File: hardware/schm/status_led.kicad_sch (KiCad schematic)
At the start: 9 parts, among them U10 SK9822-EC20, U8 SN74AHCT1G125, U9 SN74AHCT1G125

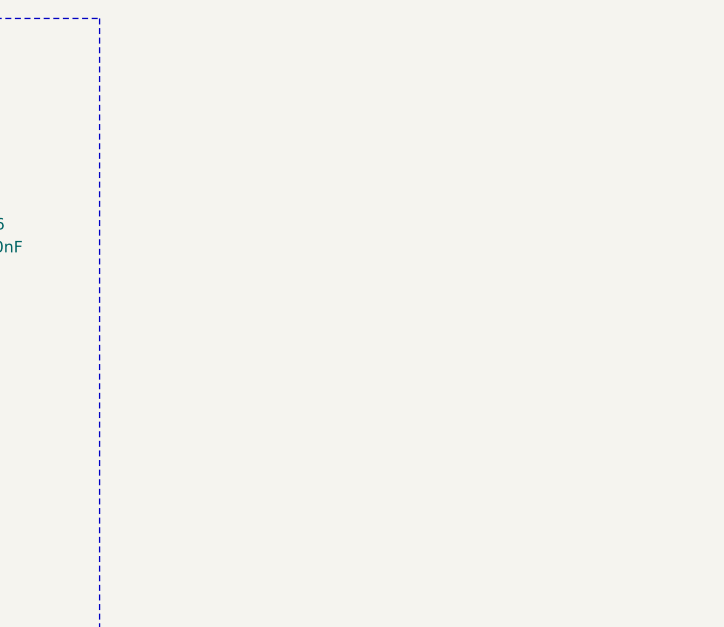
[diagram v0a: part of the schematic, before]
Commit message: feat: swap to the 74HC595 for cs expansion
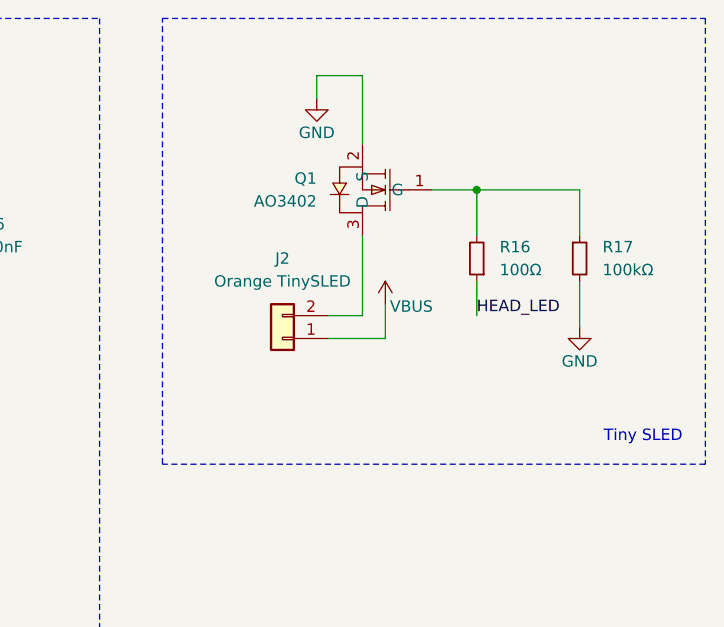
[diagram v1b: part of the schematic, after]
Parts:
- added J2: Orange TinySLED, Connector_Wire:SolderWire-0.25sqmm_1x02_P4.2mm_D0.65mm_OD1.7mm_Relief, symbol Connector_Generic:Conn_01x02
- added Q1: AO3402, Library:SOT-23_L2.9-W1.3-P1.90-LS2.4-BR, symbol Library:AO3402_C14385
- added R16: 100Ω, Resistor_SMD:R_0402_1005Metric, symbol Device:R_Small
- added R17: 100kΩ, Resistor_SMD:R_0402_1005Metric, symbol Device:R_Small
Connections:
- net GND: now also Q1.2 (S), R17.2
- new net: Q1.1 (G), R16.2, R17.1
- new net: J2.2 (Pin_2), Q1.3 (D)
- new net HEAD_LED: R16.1
- new net VBUS: J2.1 (Pin_1)
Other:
- note added: "Tiny SLED"
